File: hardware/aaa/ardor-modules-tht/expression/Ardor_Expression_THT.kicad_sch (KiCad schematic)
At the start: 29 parts, among them J101 3V3 POWER INPUT + I2C TO HOST, J302 PASSIVE PEDAL INPUT / EXCITAT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, U301 Adafruit 1085 ADS1115 QT

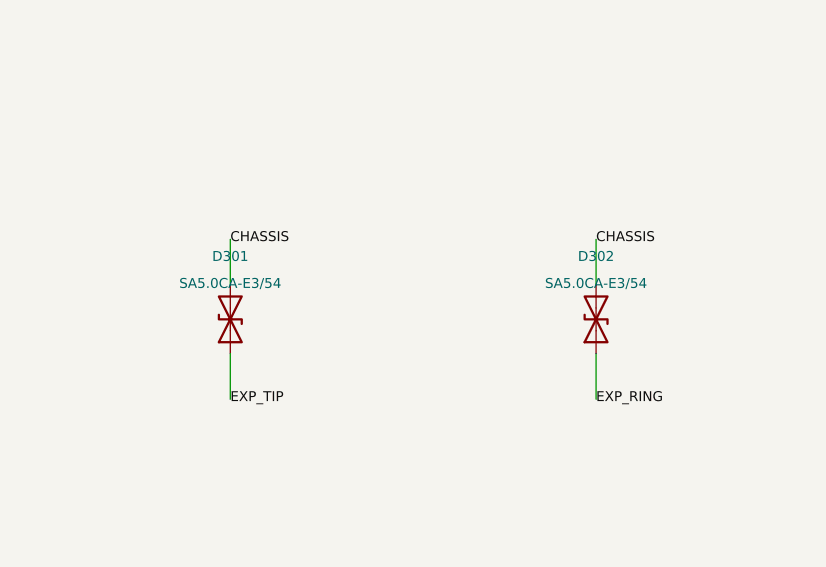
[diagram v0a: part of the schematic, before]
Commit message: fix(hardware): use Hestore TVS diodes in hand-assembly modules
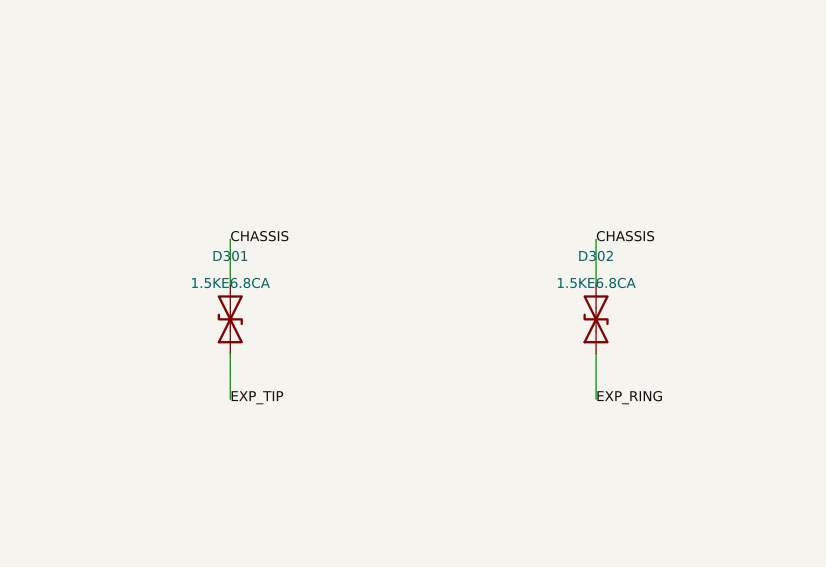
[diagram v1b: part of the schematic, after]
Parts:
- D301, D302: value SA5.0CA-E3/54 -> 1.5KE6.8CA; footprint Diode_THT:D_DO-15_P10.16mm_Horizontal -> Ardor_THT:D_TVS_DC_1.5KE_P15.24mm; MPN Vishay SA5.0CA-E3/54 -> DC Components 1.5KE6.8CA (HESTORE 100.430.71)

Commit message: feat(hardware): compact layouts and adopt Hestore module packages
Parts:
- removed JP303: JUMPER ONLY: SDA PULLUP, Connector_PinHeader_2.54mm:PinHeader_1x02_P2.54mm_Vertical, symbol Ardor:Conn_01x02
- added JP302: JUMPER ONLY: ADC ADDRESS, Connector_PinHeader_2.54mm:PinHeader_1x03_P2.54mm_Vertical, symbol Ardor:Conn_01x03
- JP303: renamed from JP302; value JUMPER ONLY: ADC ADDRESS -> JUMPER ONLY: SDA PULLUP; footprint Connector_PinHeader_2.54mm:PinHeader_1x03_P2.54mm_Vertical -> Connector_PinHeader_2.54mm:PinHeader_1x02_P2.54mm_Vertical; symbol Ardor:Conn_01x03 -> Ardor:Conn_01x02; MPN PinHeader_1x03_P2.54mm_Vertical -> PinHeader_1x02_P2.54mm_Vertical
- U301: value Adafruit 1085 ADS1115 QT -> ADS1115-M; footprint Ardor_THT:Adafruit_ADS1115_1085_STEMMA_QT -> Ardor_THT:ADS1115_M_HESTORE_10041798; MPN Adafruit 1085 (STEMMA QT revision) -> ADS1115-M (HESTORE 100.417.98)
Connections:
- net +3V3_A: now also JP302.3 (Pin_3); no longer JP303.3 (Pin_3)
- net GND: now also JP302.1 (Pin_1); no longer JP303.1 (Pin_1)
- net SDA: now also JP303.2 (Pin_2)
- net at R308.2: now also JP303.1 (Pin_1)
- net at U301.1 (ADDR): now also JP302.2 (Pin_2); no longer JP303.2 (Pin_2)
- no-connect marks 3 -> 1
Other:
- note added: "U301.2: UNUSED ALERT - LEAVE OPEN"
- note removed: "U301.2: UNUSED ALERT - LEAVE OPEN / U301.11: BREAKOUT AVDD - LEAVE OPEN / U301.12: BREAKOUT AGND - LEAVE OPEN"
